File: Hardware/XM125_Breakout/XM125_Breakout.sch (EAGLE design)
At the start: 54 parts, among them J13 SWD (DNP), J2 RIGHT_ANGLE, J3 RIGHT_ANGLE, U1 XM125, U2 RT9080-33GJ5, U3 RT9080-18GJ5, U4 CH340C, U5 ESD Diode

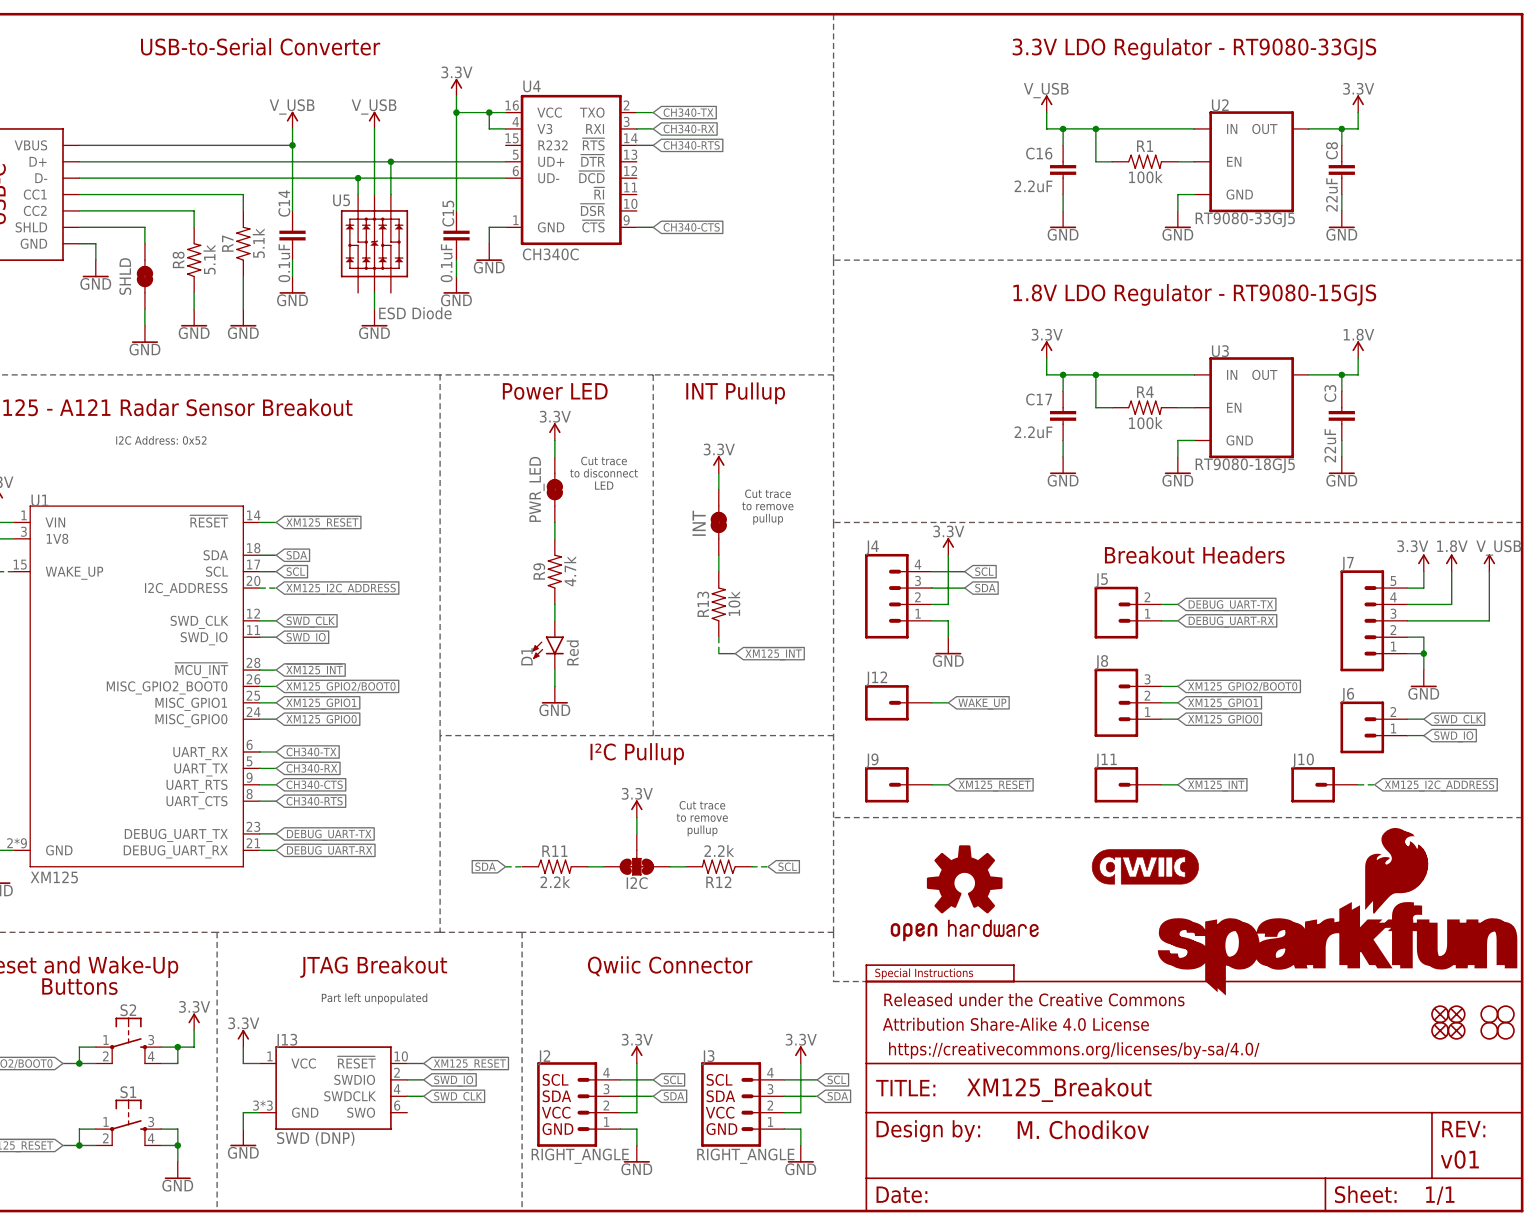
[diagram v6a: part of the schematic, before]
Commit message: Initial commit for v10 red boards; adjusted firmware files
Small changes made for board - removed EN pullups, changed button part number; no need for distance and presence file differentiation - just run with binaries in the original SDK; added STM32CubeIDEProject files for testing
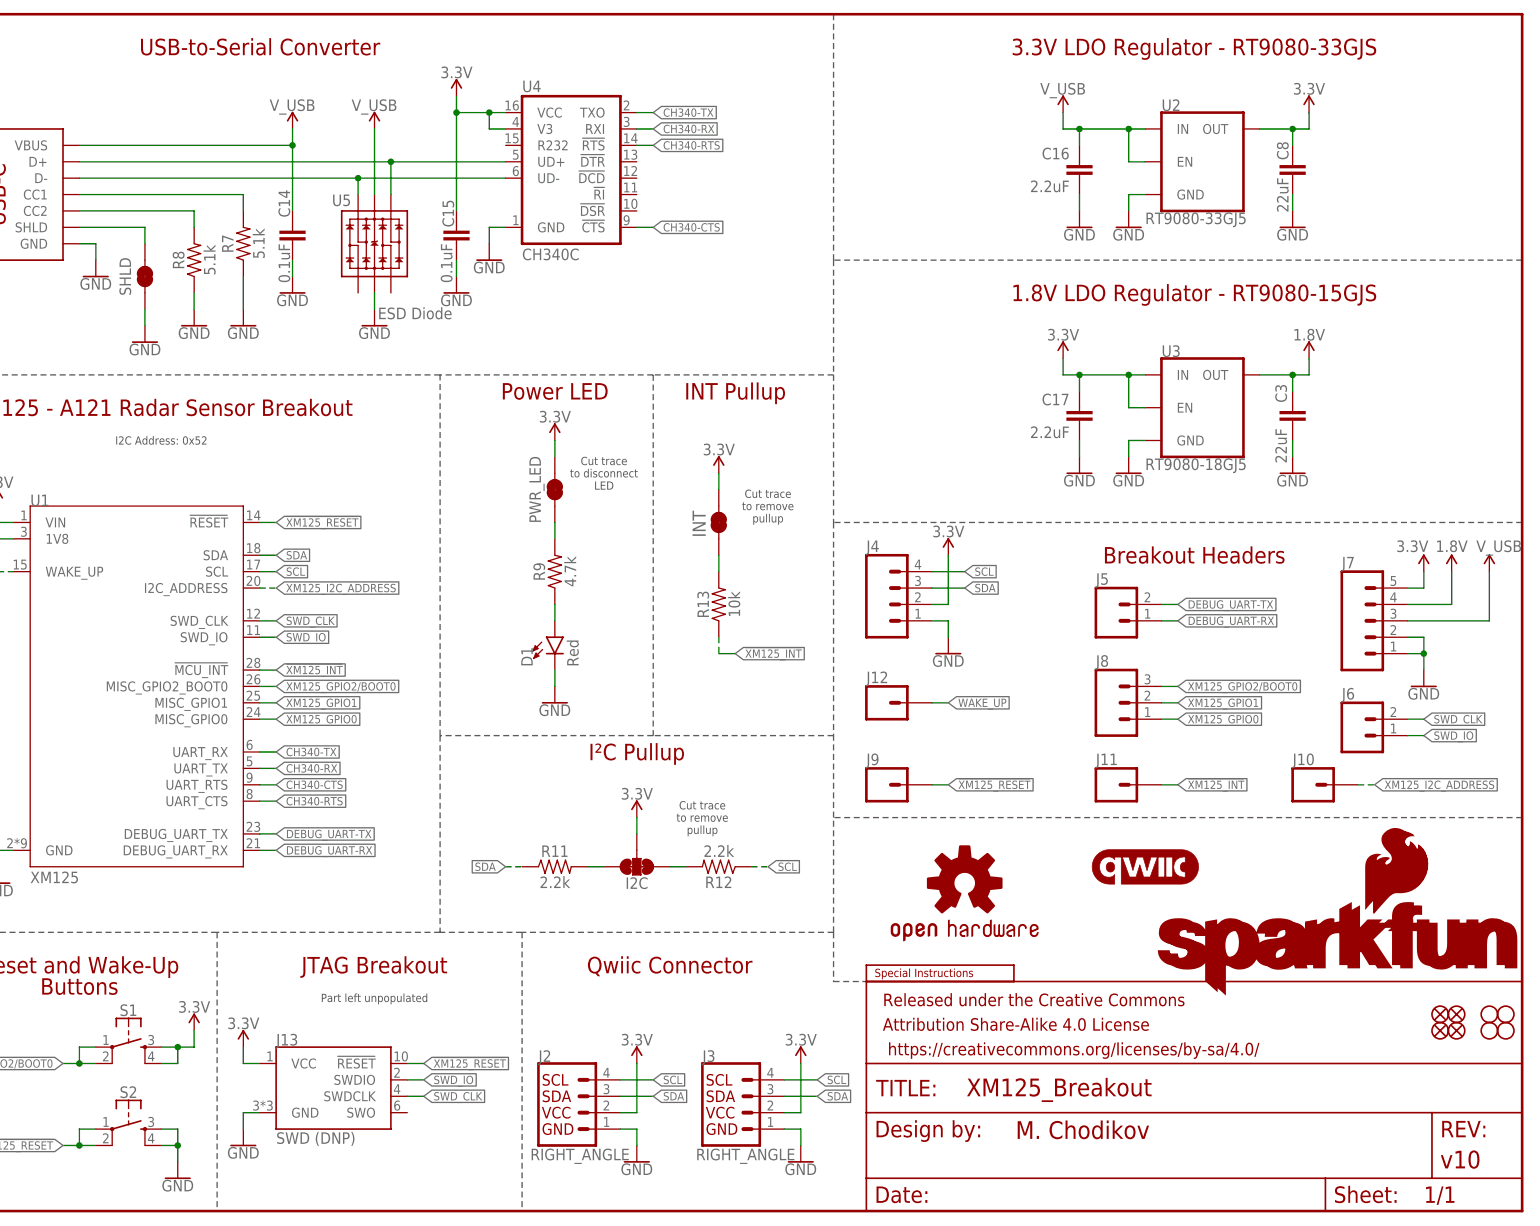
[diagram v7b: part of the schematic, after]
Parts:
- removed R1, R4: 100k, SparkFun-Resistors:100KOHM-0603-1/10W-1%
- FRAME2: REV v01 -> v10
- S1, S2: device SparkFun-Switches:MOMENTARY-SWITCH-SPST-2-SMD-5.2MM-TALL -> SparkFun-Switches:MOMENTARY-SWITCH-SPST-2-SMD-5.2MM
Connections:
- removed net N$13: R1.2, U2.EN
- removed net N$20: R4.2, U3.EN
- net !XM125_RESET: now also S2.1, S2.2; no longer S1.1, S1.2
- net 3.3V: now also S1.3, S1.4, U3.EN; no longer R4.1, S2.3, S2.4
- net GND: now also S2.3, S2.4; no longer S1.3, S1.4
- net V_USB: now also U2.EN; no longer R1.1
- net XM125_GPIO2/BOOT0: now also S1.1, S1.2; no longer S2.1, S2.2
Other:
- moved on the sheet: C16, C17, C3, C8, S1, S2, U2, U3

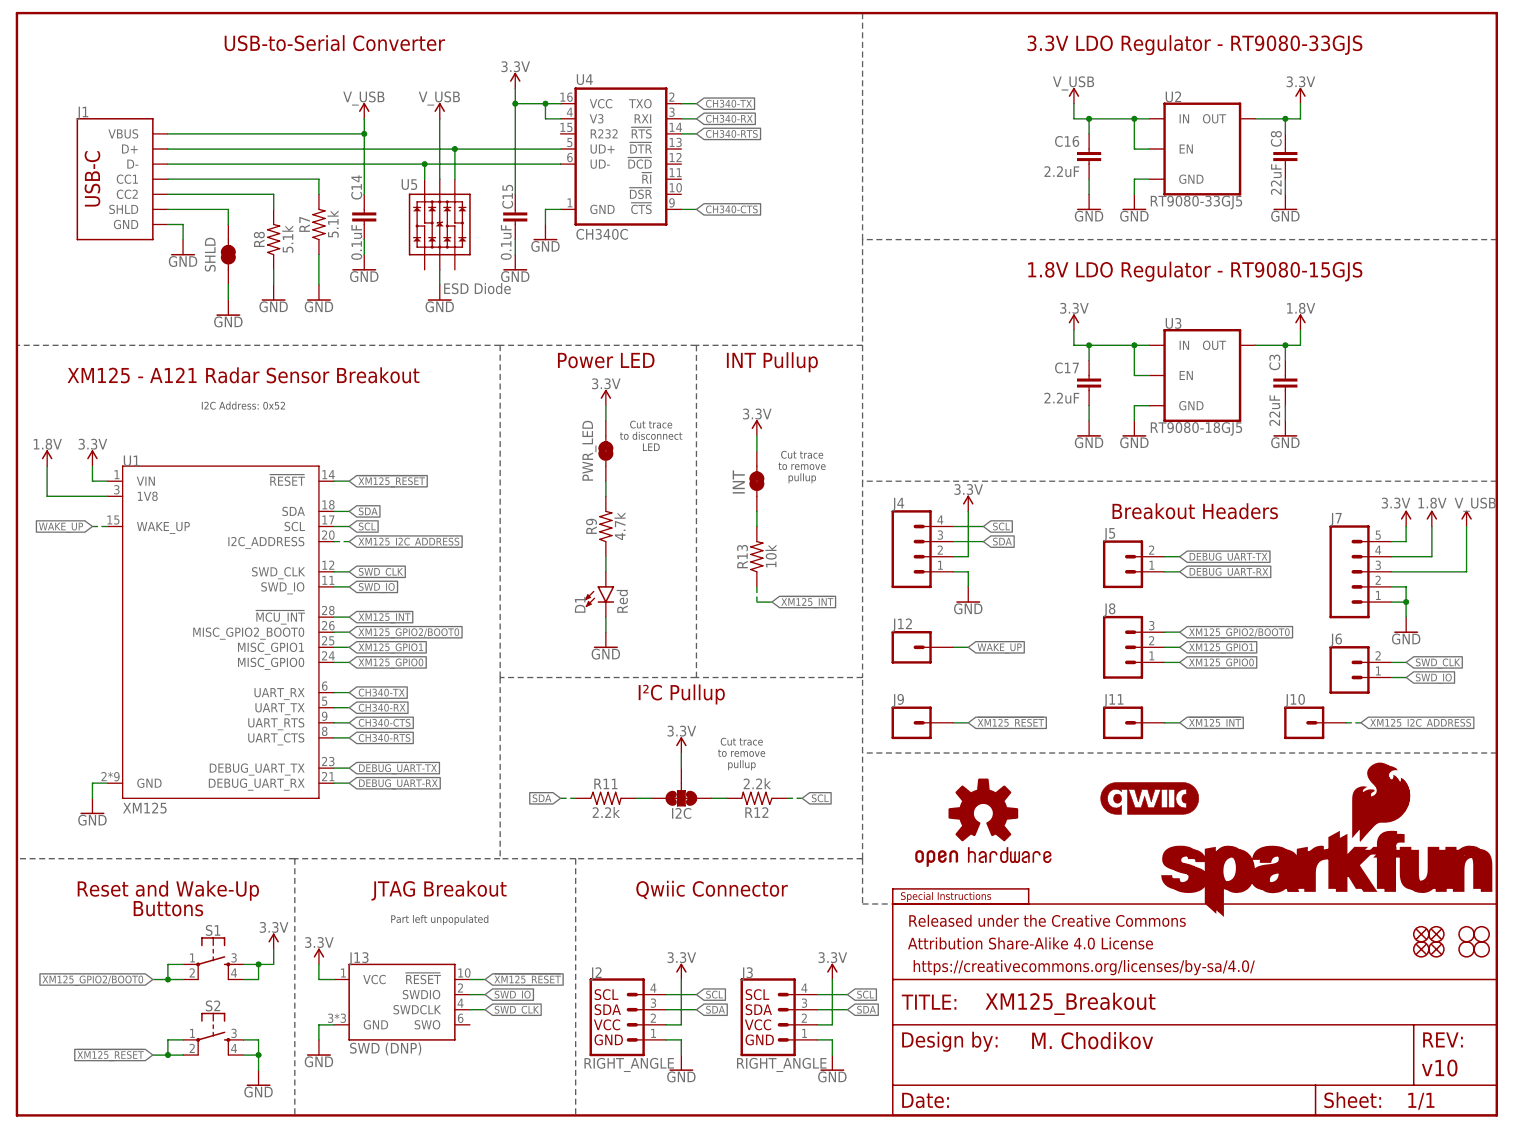
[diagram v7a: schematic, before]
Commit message: Changes for reds review completed; panel files added
Changes for review have been made; panelized files have been added
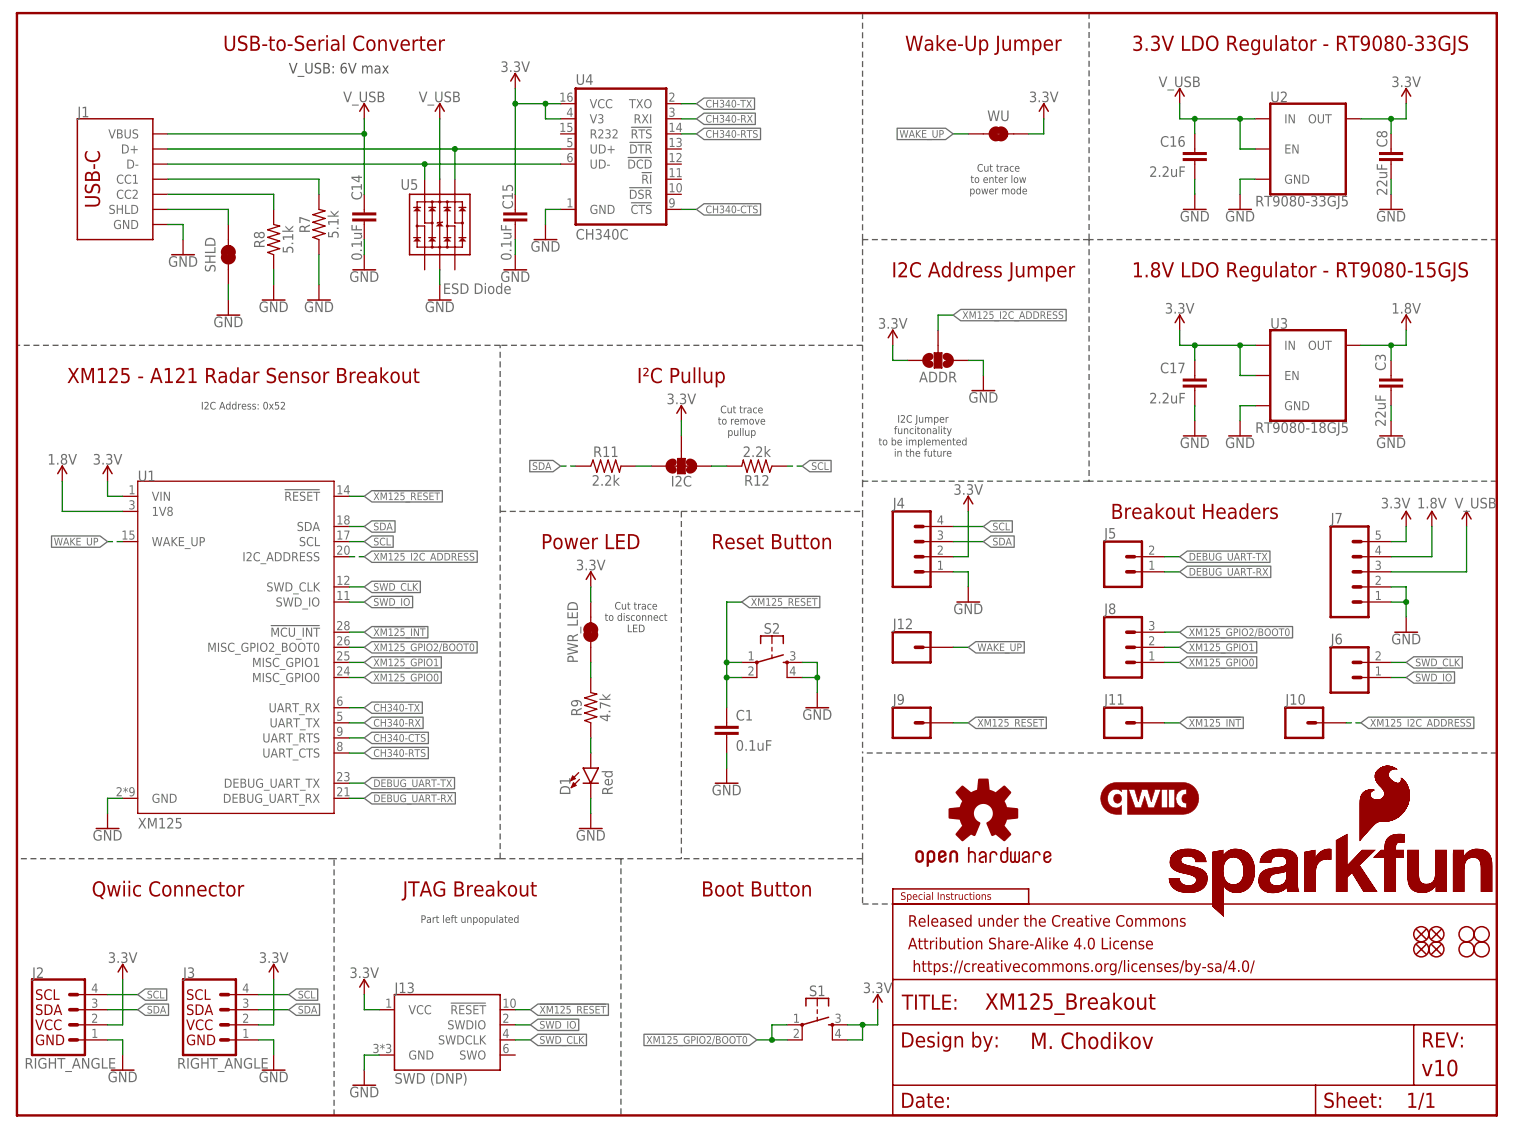
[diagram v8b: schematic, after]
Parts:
- removed JP2: JUMPER-SMT_2_NC_TRACE_SILK, SparkFun-Jumpers:JUMPER-SMT_2_NC_TRACE_SILK
- removed R13: 10k, SparkFun-Resistors:10KOHM-0603-1/10W-1%
- added ADDR: JUMPER-SMT_3_NO_SILK, SparkFun-Jumpers:JUMPER-SMT_3_NO_SILK
- added C1: 0.1uF, SparkFun-Capacitors:0.1UF-0603-25V-(+80/-20%)
- added WU: JUMPER-SMT_2_NC_TRACE_SILK, SparkFun-Jumpers:JUMPER-SMT_2_NC_TRACE_SILK
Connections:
- removed net N$18: JP2.1, R13.2
- net !XM125_INT: no longer R13.1
- net !XM125_RESET: now also C1.2
- net 3.3V: now also ADDR.3, WU.2; no longer JP2.2
- net GND: now also ADDR.1, C1.1
- net WAKE_UP: now also WU.1
- net XM125_I2C_ADDRESS: now also ADDR.2
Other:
- note added: "Boot Button"
- note added: "Cut trace to enter low power mode"
- note added: "I2C Address Jumper"
- note added: "I2C Jumper funcitonality to be implemented in the future"
- note added: "Reset Button"
- note added: "V_USB: 6V max"
- note added: "Wake-Up Jumper"
- note removed: "Buttons"
- note removed: "INT"
- note removed: "INT Pullup"
- note removed: "Reset and Wake-Up"
- moved on the sheet: C16, C17, C3, C8, D1, I2C, J13, J2, J3, PWR_LED, R11, R12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
